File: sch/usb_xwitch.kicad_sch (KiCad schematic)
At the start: 62 parts, among them J1 USB3_A, J2 USB3_A, J3 USB3_A, J4 USB3_A, J5 USB3_A, J6 USB3_A, J7 USB3_A, J8 Conn_02x05_Odd_Even, J9 C65114Copy, K1 Relay_DPDT_Panasonic_AGQ200A4H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

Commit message: update on new packaging
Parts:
- J9: value C65114Copy -> C65114
- R10, R11, R12, R9: value 240o -> 330Ω; footprint Resistor_SMD:R_0603_1608Metric_Pad0.98x0.95mm_HandSolder -> Resistor_SMD:R_0402_1005Metric_Pad0.72x0.64mm_HandSolder
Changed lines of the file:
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@@
     (in_bom yes) (on_board yes)
     (property "Reference" "J9" (id 0) (at 176.53 144.78 0))
-    (property "Value" "C65114Copy" (id 1) (at 176.53 143.51 0)
+    (property "Value" "C65114" (id 1) (at 176.53 143.51 0)
       (effects (font (size 1.27 1.27)) hide)
     )
@@
       (effects (font (size 1.27 1.27)) (justify left))
     )
-    (property "Value" "240o" (id 1) (at 246.38 142.2399 0)
-      (effects (font (size 1.27 1.27)) (justify left))
-    )
-    (property "Footprint" "Resistor_SMD:R_0603_1608Metric_Pad0.98x0.95mm_HandSolder" (id 2) (at 244.856 141.224 90)
-      (effects (font (size 1.27 1.27)) hide)
-    )
-    (property "Datasheet" "https://datasheet.lcsc.com/lcsc/2206010100_UNI-ROYAL-Uniroyal-Elec-0603WAF2400T5E_C23350.pdf" (id 3) (at 243.84 140.97 0)
+    (property "Value" "330Ω" (id 1) (at 246.38 142.2399 0)
+      (effects (font (size 1.27 1.27)) (justify left))
+    )
+    (property "Footprint" "Resistor_SMD:R_0402_1005Metric_Pad0.72x0.64mm_HandSolder" (id 2) (at 244.856 141.224 90)
+      (effects (font (size 1.27 1.27)) hide)
+    )
+    (property "Datasheet" "https://datasheet.lcsc.com/lcsc/2205311900_UNI-ROYAL-Uniroyal-Elec-0402WGF3300TCE_C25104.pdf" (id 3) (at 243.84 140.97 0)
       (effects (font (size 1.27 1.27)) hide)
     )
@@
       (effects (font (size 1.27 1.27)) (justify left))
     )
-    (property "Value" "240o" (id 1) (at 255.27 142.2399 0)
-      (effects (font (size 1.27 1.27)) (justify left))
-    )
-    (property "Footprint" "Resistor_SMD:R_0603_1608Metric_Pad0.98x0.95mm_HandSolder" (id 2) (at 253.746 141.224 90)
-      (effects (font (size 1.27 1.27)) hide)
-    )
-    (property "Datasheet" "https://datasheet.lcsc.com/lcsc/2206010100_UNI-ROYAL-Uniroyal-Elec-0603WAF2400T5E_C23350.pdf" (id 3) (at 252.73 140.97 0)
+    (property "Value" "330Ω" (id 1) (at 255.27 142.2399 0)
+      (effects (font (size 1.27 1.27)) (justify left))
+    )
+    (property "Footprint" "Resistor_SMD:R_0402_1005Metric_Pad0.72x0.64mm_HandSolder" (id 2) (at 253.746 141.224 90)
+      (effects (font (size 1.27 1.27)) hide)
+    )
+    (property "Datasheet" "https://datasheet.lcsc.com/lcsc/2205311900_UNI-ROYAL-Uniroyal-Elec-0402WGF3300TCE_C25104.pdf" (id 3) (at 252.73 140.97 0)
       (effects (font (size 1.27 1.27)) hide)
     )
@@
       (effects (font (size 1.27 1.27)) (justify left))
     )
-    (property "Value" "240o" (id 1) (at 237.49 142.2399 0)
-      (effects (font (size 1.27 1.27)) (justify left))
-    )
-    (property "Footprint" "Resistor_SMD:R_0603_1608Metric_Pad0.98x0.95mm_HandSolder" (id 2) (at 235.966 141.224 90)
-      (effects (font (size 1.27 1.27)) hide)
-    )
-    (property "Datasheet" "https://datasheet.lcsc.com/lcsc/2206010100_UNI-ROYAL-Uniroyal-Elec-0603WAF2400T5E_C23350.pdf" (id 3) (at 234.95 140.97 0)
+    (property "Value" "330Ω" (id 1) (at 237.49 142.2399 0)
+      (effects (font (size 1.27 1.27)) (justify left))
+    )
+    (property "Footprint" "Resistor_SMD:R_0402_1005Metric_Pad0.72x0.64mm_HandSolder" (id 2) (at 235.966 141.224 90)
+      (effects (font (size 1.27 1.27)) hide)
+    )
+    (property "Datasheet" "https://datasheet.lcsc.com/lcsc/2205311900_UNI-ROYAL-Uniroyal-Elec-0402WGF3300TCE_C25104.pdf" (id 3) (at 234.95 140.97 0)
       (effects (font (size 1.27 1.27)) hide)
     )
@@
       (effects (font (size 1.27 1.27)) (justify left))
     )
-    (property "Value" "240o" (id 1) (at 264.16 142.2399 0)
-      (effects (font (size 1.27 1.27)) (justify left))
-    )
-    (property "Footprint" "Resistor_SMD:R_0603_1608Metric_Pad0.98x0.95mm_HandSolder" (id 2) (at 262.636 141.224 90)
-      (effects (font (size 1.27 1.27)) hide)
-    )
-    (property "Datasheet" "https://datasheet.lcsc.com/lcsc/2206010100_UNI-ROYAL-Uniroyal-Elec-0603WAF2400T5E_C23350.pdf" (id 3) (at 261.62 140.97 0)
+    (property "Value" "330Ω" (id 1) (at 264.16 142.2399 0)
+      (effects (font (size 1.27 1.27)) (justify left))
+    )
+    (property "Footprint" "Resistor_SMD:R_0402_1005Metric_Pad0.72x0.64mm_HandSolder" (id 2) (at 262.636 141.224 90)
+      (effects (font (size 1.27 1.27)) hide)
+    )
+    (property "Datasheet" "https://datasheet.lcsc.com/lcsc/2205311900_UNI-ROYAL-Uniroyal-Elec-0402WGF3300TCE_C25104.pdf" (id 3) (at 261.62 140.97 0)
       (effects (font (size 1.27 1.27)) hide)
     )
@@
     )
     (path "/05076186-aa8c-4422-942d-c35ba457f49e"
-      (reference "J9") (unit 1) (value "C65114Copy") (footprint "Connector_PinHeader_2.54mm:PinHeader_2x03_P2.54mm_Vertical")
+      (reference "J9") (unit 1) (value "C65114") (footprint "Connector_PinHeader_2.54mm:PinHeader_2x03_P2.54mm_Vertical")
     )
     (path "/1ad93629-9c29-44d2-a5f4-c38945e05903"
@@
     )
     (path "/ab7d4282-2b8b-4740-9065-f14f397a74b9"
-      (reference "R9") (unit 1) (value "240o") (footprint "Resistor_SMD:R_0603_1608Metric_Pad0.98x0.95mm_HandSolder")
+      (reference "R9") (unit 1) (value "330Ω") (footprint "Resistor_SMD:R_0402_1005Metric_Pad0.72x0.64mm_HandSolder")
     )
     (path "/2077c3fe-878a-4115-9c7a-2c8d1e775f8e"
-      (reference "R10") (unit 1) (value "240o") (footprint "Resistor_SMD:R_0603_1608Metric_Pad0.98x0.95mm_HandSolder")
+      (reference "R10") (unit 1) (value "330Ω") (footprint "Resistor_SMD:R_0402_1005Metric_Pad0.72x0.64mm_HandSolder")
     )
     (path "/61fa168a-7cd2-49f5-bf3a-d81e261300ae"
-      (reference "R11") (unit 1) (value "240o") (footprint "Resistor_SMD:R_0603_1608Metric_Pad0.98x0.95mm_HandSolder")
+      (reference "R11") (unit 1) (value "330Ω") (footprint "Resistor_SMD:R_0402_1005Metric_Pad0.72x0.64mm_HandSolder")
     )
     (path "/ef6cee14-a255-4a4a-a342-1e947e99208d"
-      (reference "R12") (unit 1) (value "240o") (footprint "Resistor_SMD:R_0603_1608Metric_Pad0.98x0.95mm_HandSolder")
+      (reference "R12") (unit 1) (value "330Ω") (footprint "Resistor_SMD:R_0402_1005Metric_Pad0.72x0.64mm_HandSolder")
     )
     (path "/af047df2-64d9-4941-aac1-dbe0147cb1ee"

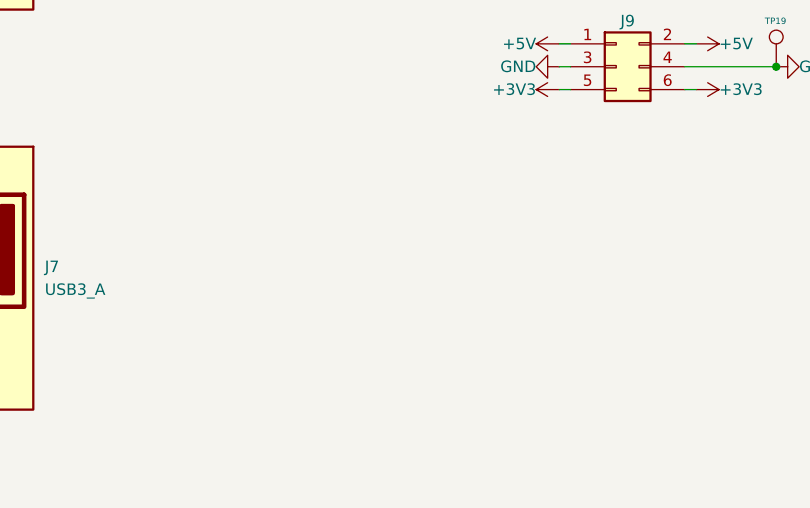
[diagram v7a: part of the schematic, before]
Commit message: added rp2040 lib symbols; updated to 2 sch pages
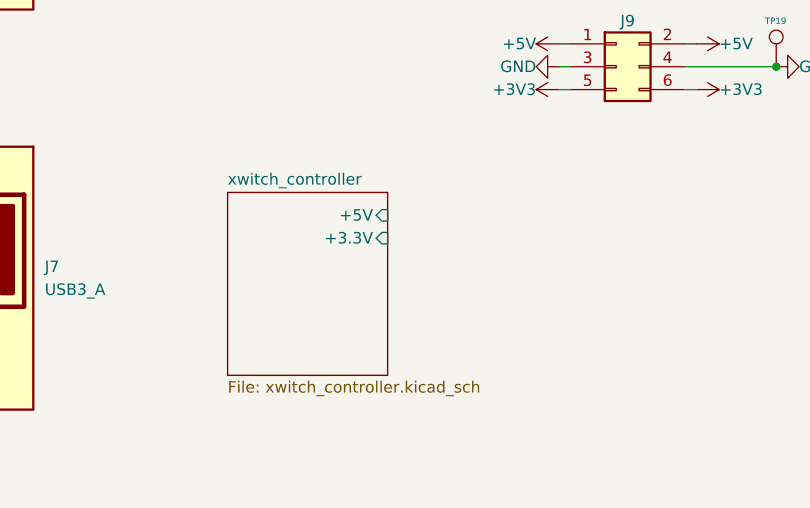
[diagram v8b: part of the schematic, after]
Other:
- added sheet xwitch_controller (xwitch_controller.kicad_sch)
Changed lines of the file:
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@@
     (pin "1")
+  )
+  (sheet (at 132.08 163.83) (size 17.78 20.32) (fields_autoplaced)
+    (stroke (width 0.1524) (type solid) (color 0 0 0 0))
+    (fill (color 0 0 0 0.0000))
+    (property "Sheet name" "xwitch_controller" (id 0) (at 132.08 163.1184 0)
+      (effects (font (size 1.27 1.27)) (justify left bottom))
+    )
+    (property "Sheet file" "xwitch_controller.kicad_sch" (id 1) (at 132.08 184.7346 0)
+      (effects (font (size 1.27 1.27)) (justify left top))
+    )
+    (pin "+5V" input (at 149.86 166.37 0)
+      (effects (font (size 1.27 1.27)) (justify right))
+    )
+    (pin "+3.3V" input (at 149.86 168.91 0)
+      (effects (font (size 1.27 1.27)) (justify right))
+    )
   )
   (sheet_instances
     (path "/" (page "1"))
+    (path "/71a687af-7ac4-4373-9578-b04c8798d7c9" (page "2"))
   )
   (symbol_instances
@@
       (reference "#PWR0103") (unit 1) (value "GND") (footprint "")
     )
+    (path "/71a687af-7ac4-4373-9578-b04c8798d7c9/1286e70f-88dd-4928-a7ad-fad2a4af637f"
+      (reference "#PWR?") (unit 1) (value "+3V3") (footprint "")
+    )
+    (path "/71a687af-7ac4-4373-9578-b04c8798d7c9/1366a3b4-a0f2-486f-ad7d-bc13b9074e54"
+      (reference "#PWR?") (unit 1) (value "GND") (footprint "")
+    )
+    (path "/71a687af-7ac4-4373-9578-b04c8798d7c9/7262cc2d-b219-49cf-9e8f-7beb9defa079"
+      (reference "#PWR?") (unit 1) (value "+5V") (footprint "")
+    )
     (path "/8bf33d1e-be8e-4a75-bd6d-ec65058ec7e7"
